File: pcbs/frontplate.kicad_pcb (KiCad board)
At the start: 2 copper layers, 133.3 x 91.7 mm, 5 parts

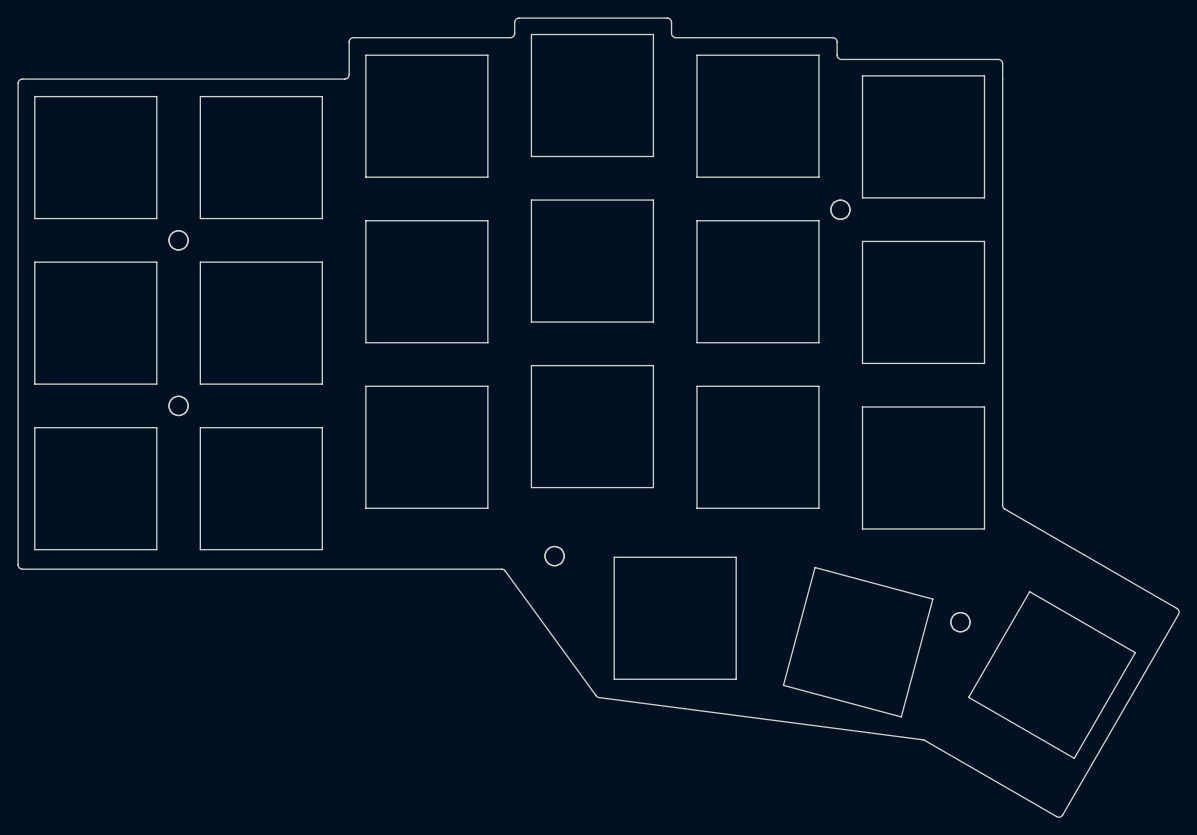
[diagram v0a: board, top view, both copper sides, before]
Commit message: build: regenerate outlines and PCBs using Ergogen v4.3.0
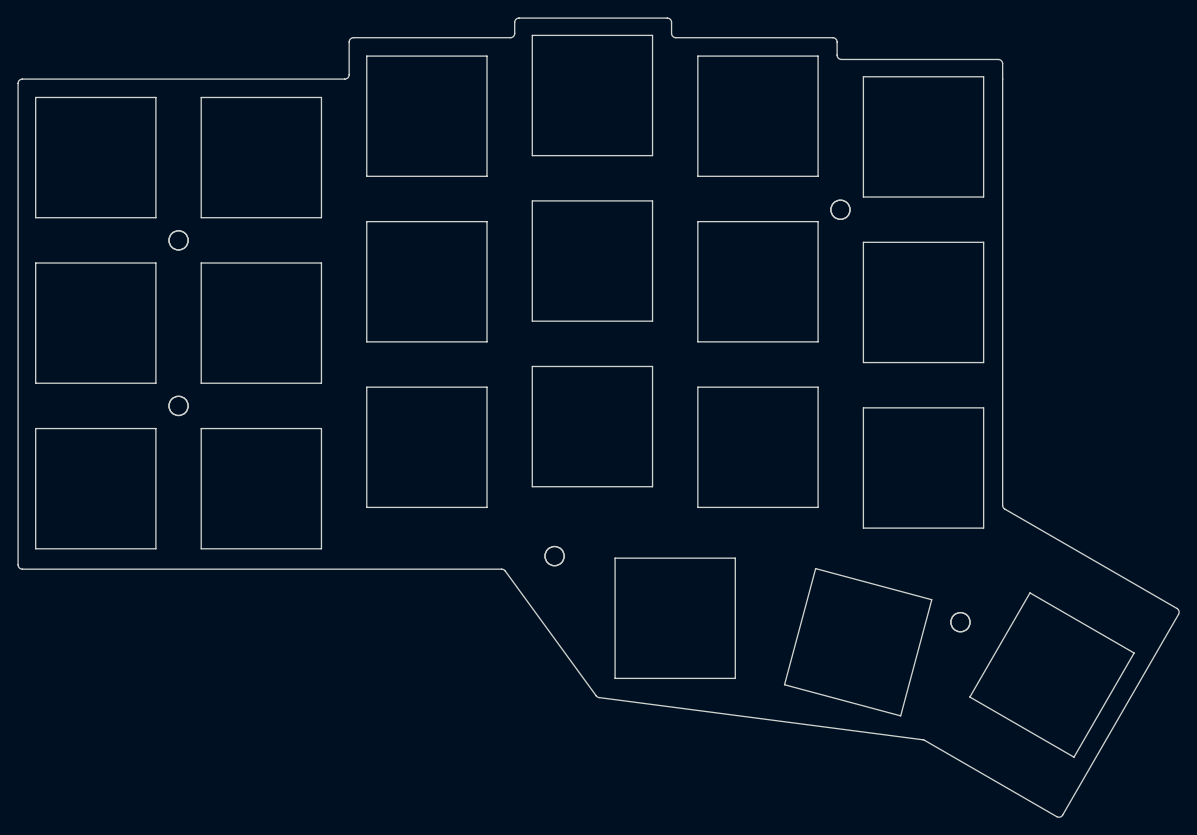
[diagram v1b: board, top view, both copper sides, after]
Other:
- outline, holes or cut-outs redrawn

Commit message: build: generate PCB layouts, routing, gerbers, and preview images
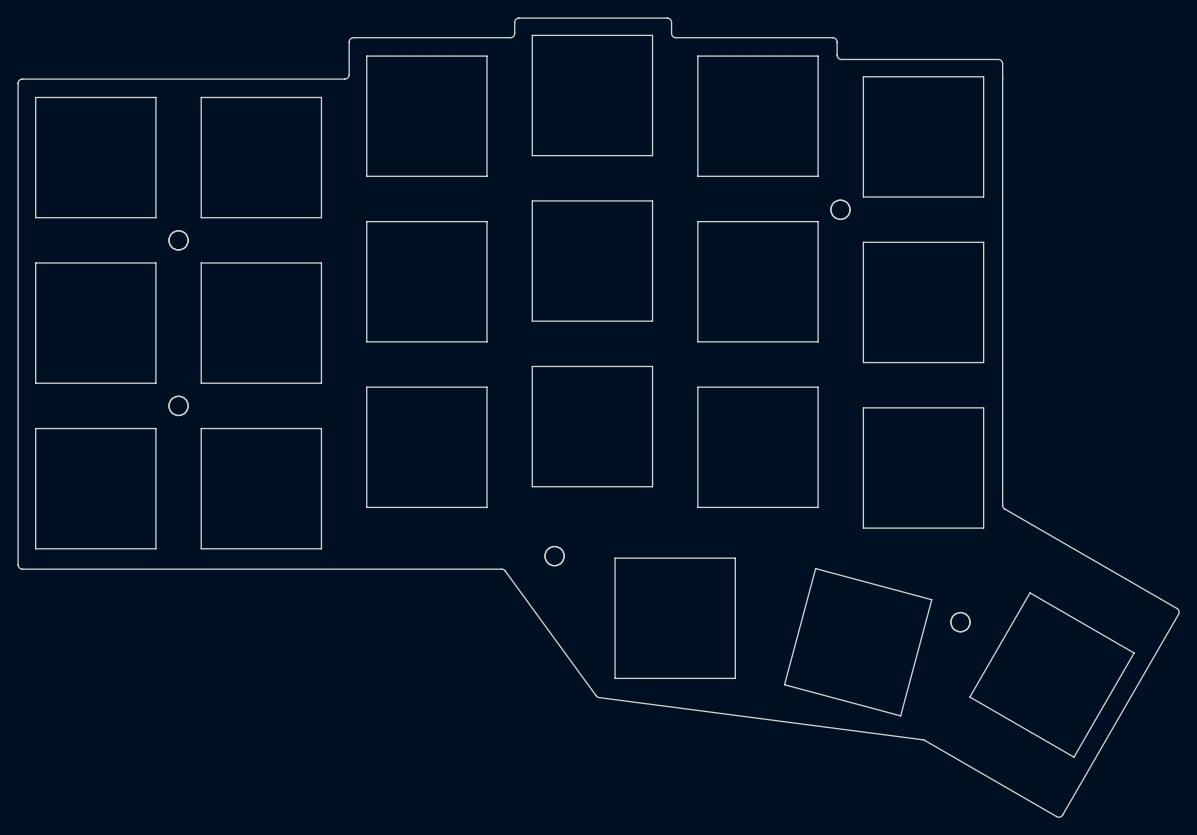
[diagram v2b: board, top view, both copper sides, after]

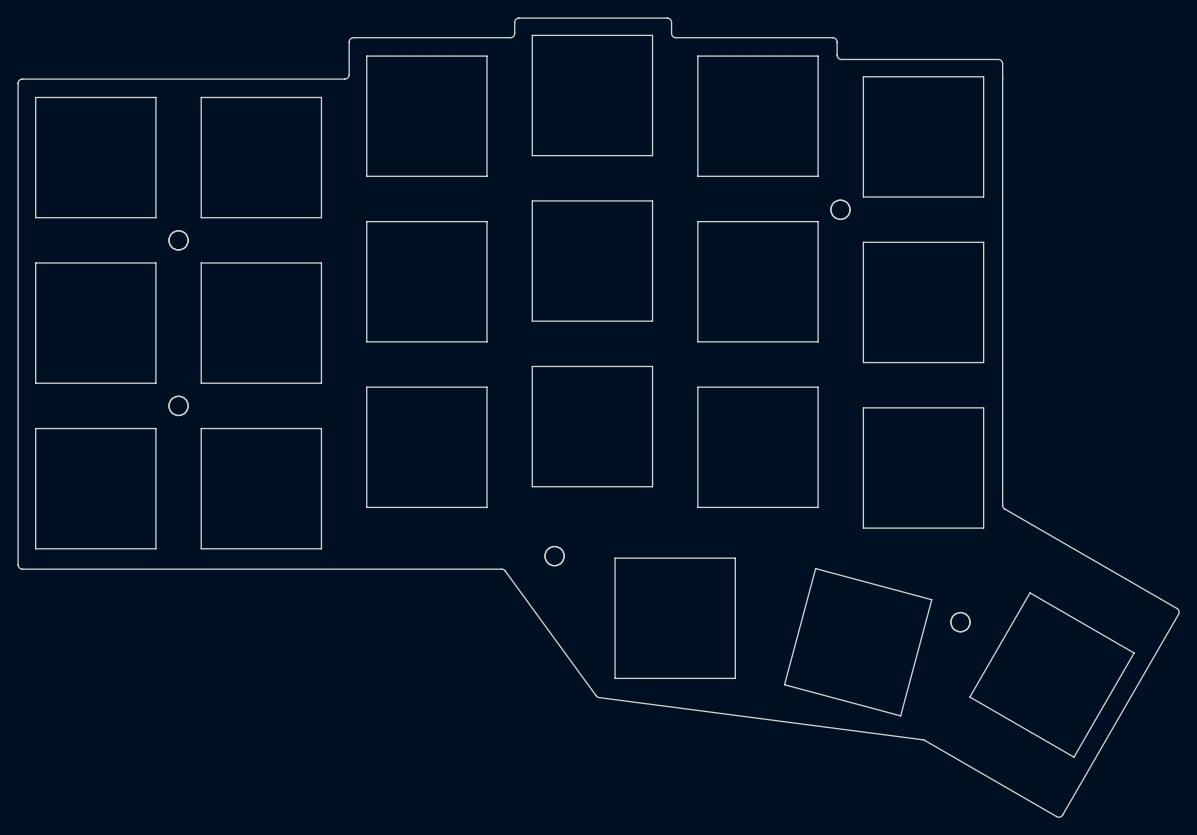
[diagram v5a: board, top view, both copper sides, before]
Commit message: Refresh generated Corney Island boards and KiCad projects
Regenerate with KiCad 9.0.7+1 and the Freerouting fixes at 48c969dd, using
neckdown and fanout disabled, one worker, and optimization enabled. The fixed
JAR was mounted over the pinned image for this local build.

Both boards have zero missing connections after SES import. Wireless has no
DRC errors; wired retains the 16 source copper-edge errors. The frontplate
still fails its outline check, so failed-board fabrication exports are skipped.

Regenerate wireless fabrication outputs after the unfiltered KiCad DRC passes,
bypassing KiBot's subsequent HTML-report parsing failure. Include the generated
project settings with the boards, reports, images, and archives.
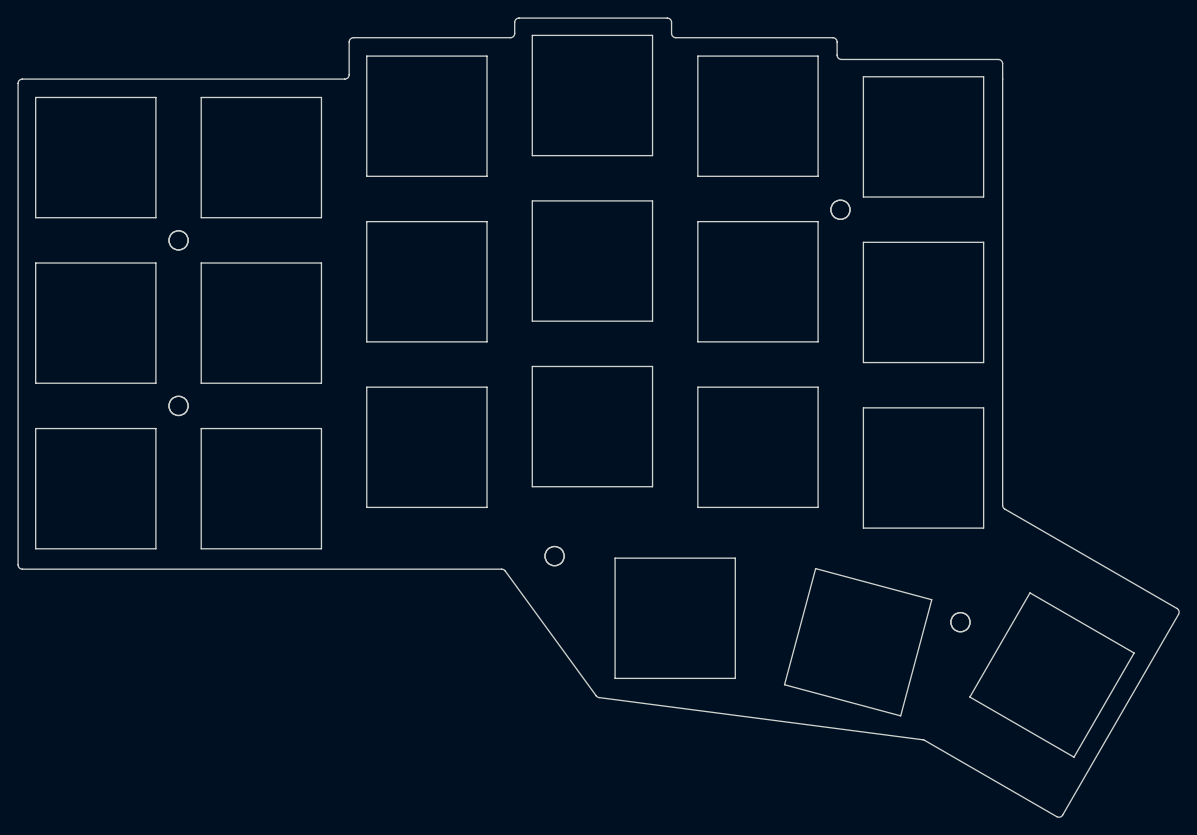
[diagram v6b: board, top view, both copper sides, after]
